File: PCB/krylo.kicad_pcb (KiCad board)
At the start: 2 copper layers, 135.3 x 87.6 mm, 52 parts, among them SW1 Switch, SW10 Switch, SW11 Switch, SW12 Switch, SW13 Switch, SW14 Switch, SW15 Switch, SW16 Switch, SW2 Switch, SW3 Switch, SW4 Switch, SW5 Switch, SW6 Switch, SW7 Switch, SW8 Switch, SW9 Switch, U1 nice_nano

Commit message: Fix: added the missing connection of the left backside power jumper
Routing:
- net Net-(SW_PWR1-B_back): track 27.3 -> 29.0 mm, vias 1 -> 2
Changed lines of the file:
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@@
 		)
 		(fp_line
-			(start 1.999998 -4.25)
+			(start 1.999997 -4.25)
 			(end 2 -7.7)
 			(stroke
@@
 		(fp_line
 			(start -1.5 -3.7)
-			(end 0.999998 -3.7)
+			(end 0.999997 -3.7)
 			(stroke
 				(width 0.1)
@@
 		)
 		(fp_arc
-			(start 0.999998 -3.7)
+			(start 0.999997 -3.7)
 			(mid 2.06066 -3.26066)
 			(end 2.5 -2.2)
@@
 		(net "Net-(SW_PWR1-B_back)")
 	)
+	(segment
+		(start 108.305185 105.254425)
+		(end 107.05038 103.99962)
+		(width 0.25)
+		(layer "F.Cu")
+		(net "Net-(SW_PWR1-B_back)")
+	)
+	(via
+		(at 107.05038 103.99962)
+		(size 0.6)
+		(drill 0.3)
+		(layers "F.Cu" "B.Cu")
+		(net "Net-(SW_PWR1-B_back)")
+	)
 	(via
 		(at 104.3 82.25)
@@
 	(segment
 		(start 108.325 105.27424)
-		(end 107.025 103.97424)
+		(end 107.05038 103.99962)
 		(width 0.25)
 		(layer "B.Cu")
@@
 		(width 0.25)
 		(layer "B.Cu")
+		(net "Net-(SW_PWR1-B_back)")
+	)
+	(segment
+		(start 107.05038 103.99962)
+		(end 107.025 103.97424)
+		(width 0.25)
+		(layer "B.Cu")

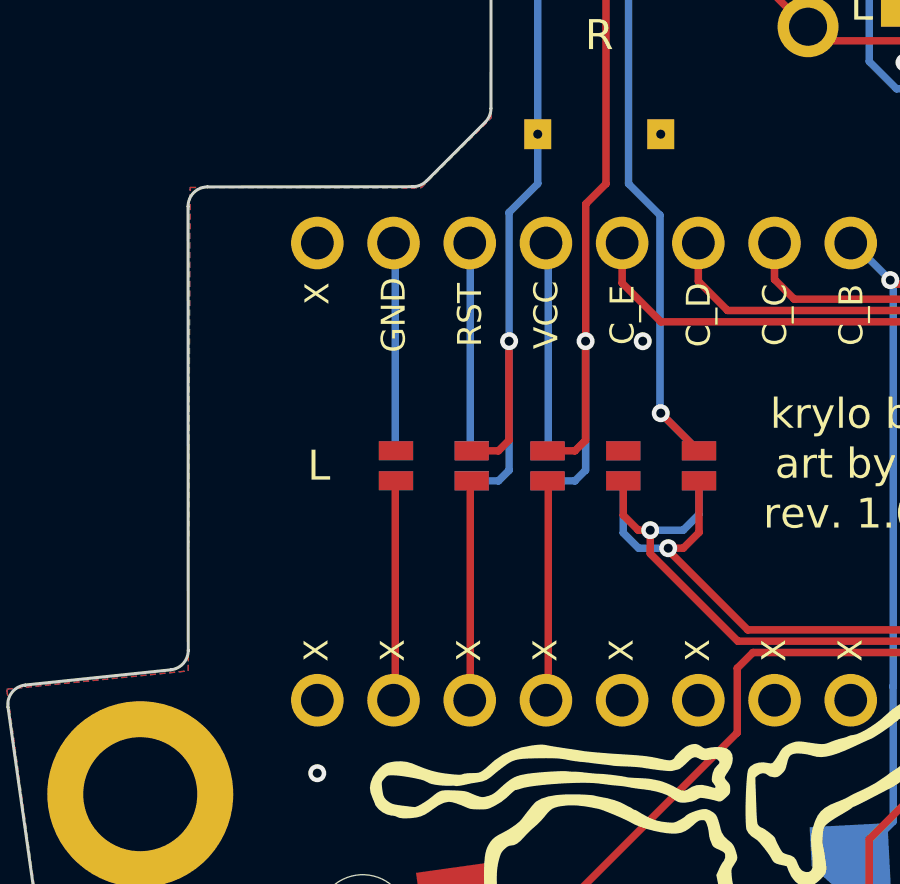
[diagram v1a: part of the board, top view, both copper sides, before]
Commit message: Fix: power goes to the VBAT pin instead of the EXT_GCC, this way we fix the inability to read the battery values by the MCU and avoid the soft off charge drain issue
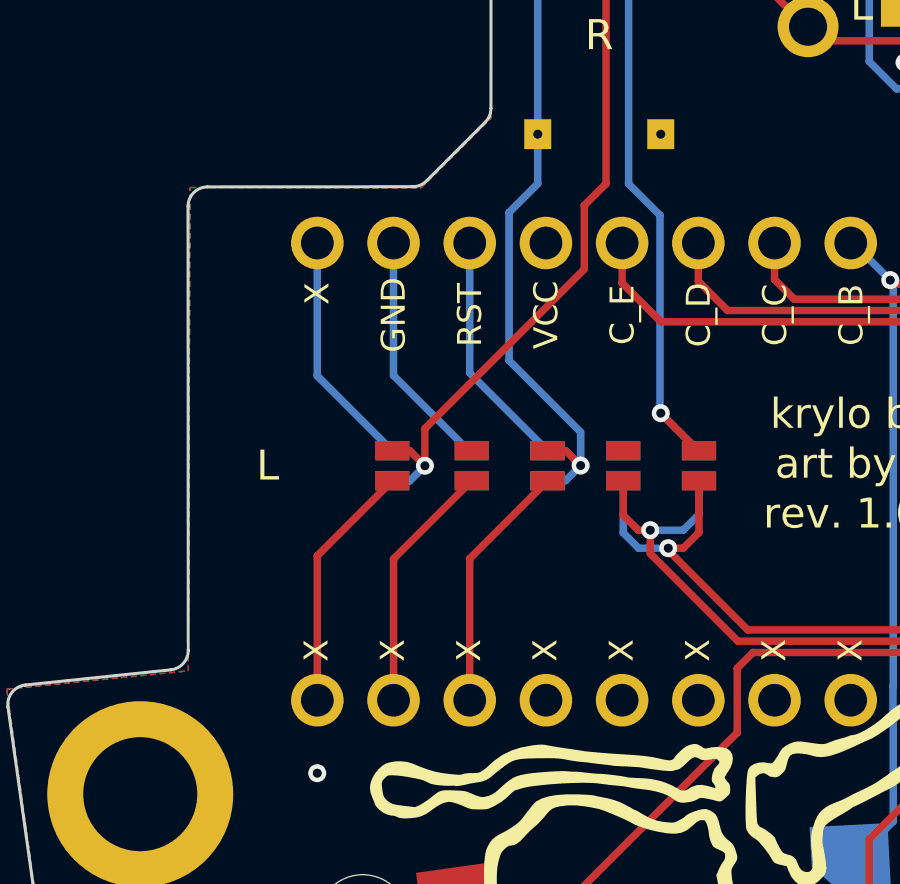
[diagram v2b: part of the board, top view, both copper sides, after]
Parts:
- moved JP9 5.18 mm to (98.1, 105.7)
- moved JP10 5.17 mm to (98.1, 105.8)
- moved JP7 2.53 mm to (103.3, 105.7)
- moved JP8 2.53 mm to (103.3, 105.8)
- moved JP5 2.52 mm to (100.7, 105.7)
- moved JP6 2.52 mm to (100.7, 105.7)
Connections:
- U1 pad 1: unconnected-(U1-D1/P0.06-Pad1) -> /+BATT_{indirect}
- U1 pad 13: unconnected-(U1-VBAT-Pad13) -> /+BATT_{indirect}
- U1 pad 16: /+BATT_{indirect} -> unconnected-(U1-EXT_VCC-Pad16)
- U1 pad 4: /+BATT_{indirect} -> unconnected-(U1-GND-Pad4)
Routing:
- net /RESET_{indirect}: track 13.7 -> 16.4 mm
- net RESET: track 24.3 -> 21.8 mm
- net /GND_{indirect}: track 14.0 -> 16.4 mm
- net /+BATT_{indirect}: track 13.8 -> 16.2 mm
- net +BATT: track 33.1 -> 31.7 mm
- net GND: vias 4 -> 3

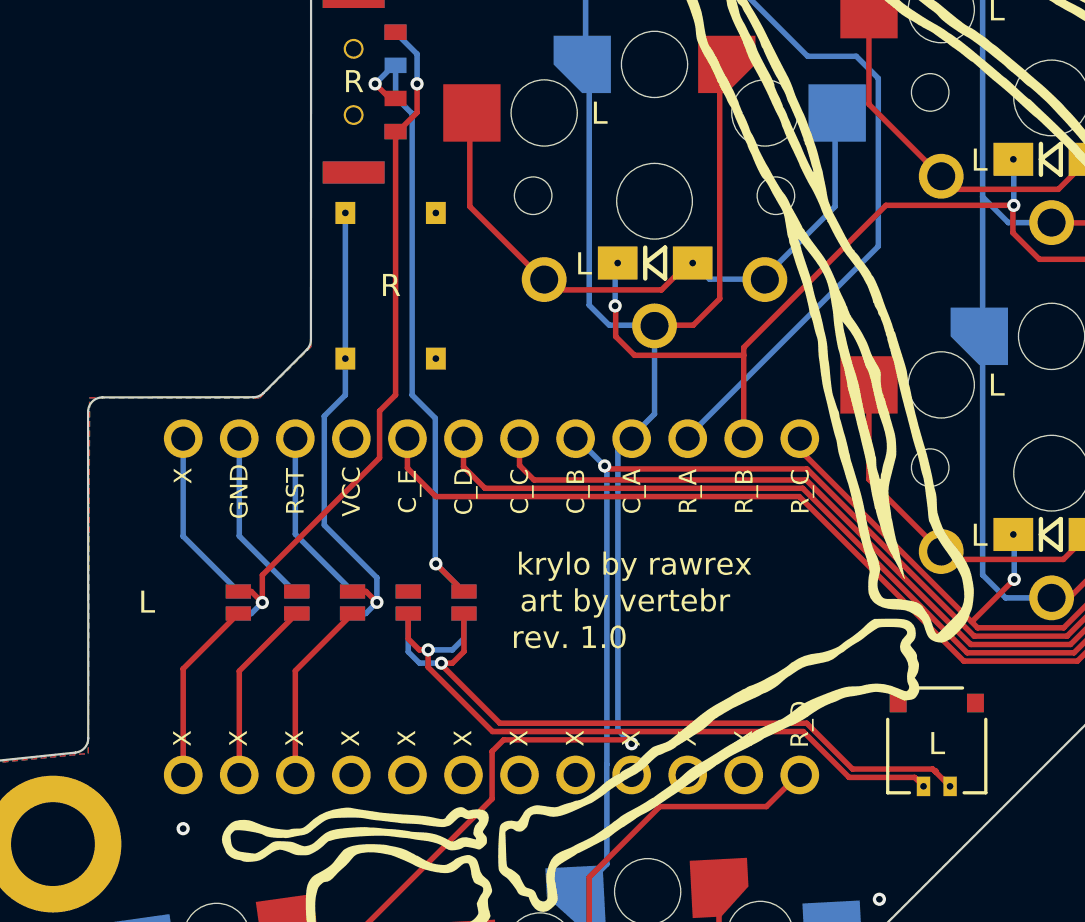
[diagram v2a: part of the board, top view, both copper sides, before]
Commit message: Jumper pads narrowed down and track clean up
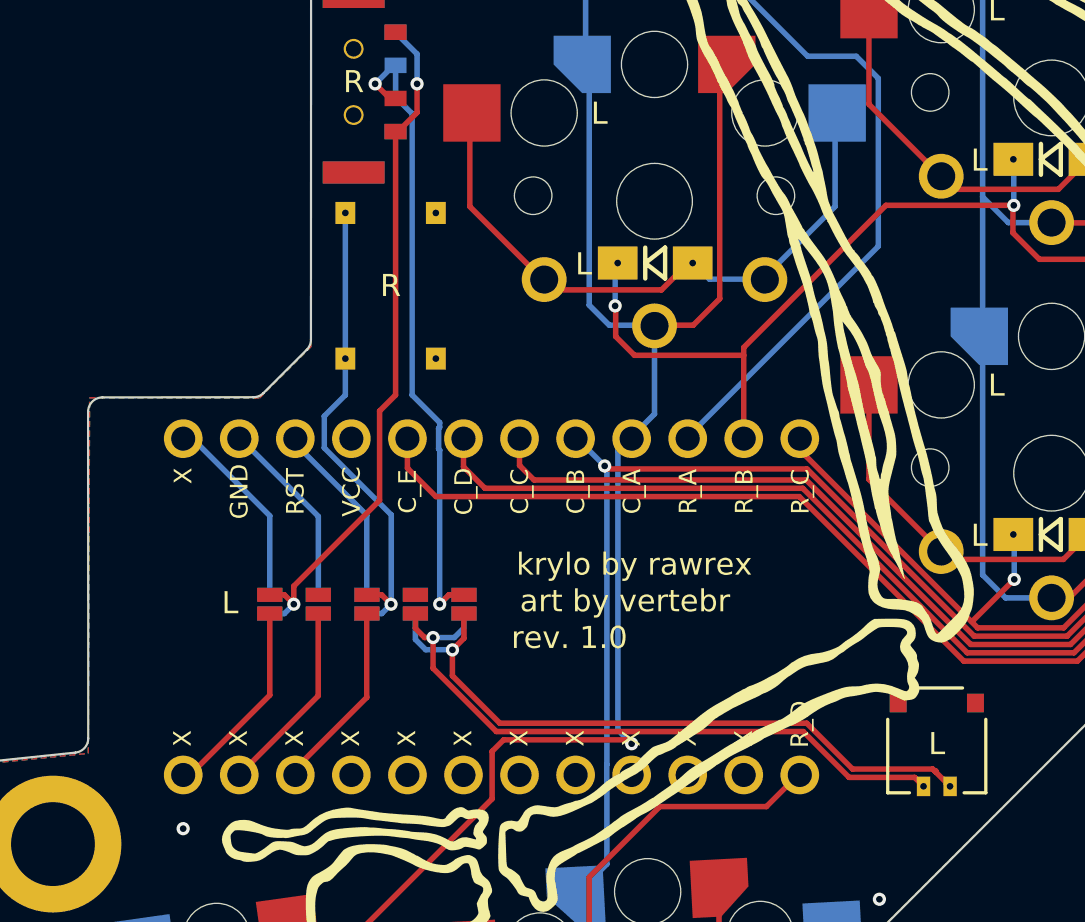
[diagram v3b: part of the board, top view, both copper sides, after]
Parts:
- BT1: value MOLEX_C -> Molex
- H1, H2, H3, H4: value Mount -> SMTSO2020MTJ_M2
- moved JP10 1.43 mm to (99.5, 105.9)
- moved JP9 1.43 mm to (99.5, 105.8)
- moved JP6 0.99 mm to (101.7, 105.9)
- moved JP5 0.98 mm to (101.7, 105.8)
- moved JP8 0.67 mm to (103.9, 105.9)
- moved JP7 0.65 mm to (103.9, 105.8)
- moved JP1 0.33 mm to (106.1, 105.8)
- moved JP4 0.33 mm to (106.1, 105.8)
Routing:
- net /PAD1: track 31.8 -> 30.7 mm
- net /PAD2: track 30.7 -> 29.7 mm
- net /+BATT_{indirect}: track 16.2 -> 17.1 mm
- net Net-(SW_PWR1-B_back): track 29.0 -> 30.0 mm
- net /GND_{indirect}: track 16.4 -> 17.2 mm
- net +BATT: track 31.7 -> 31.1 mm

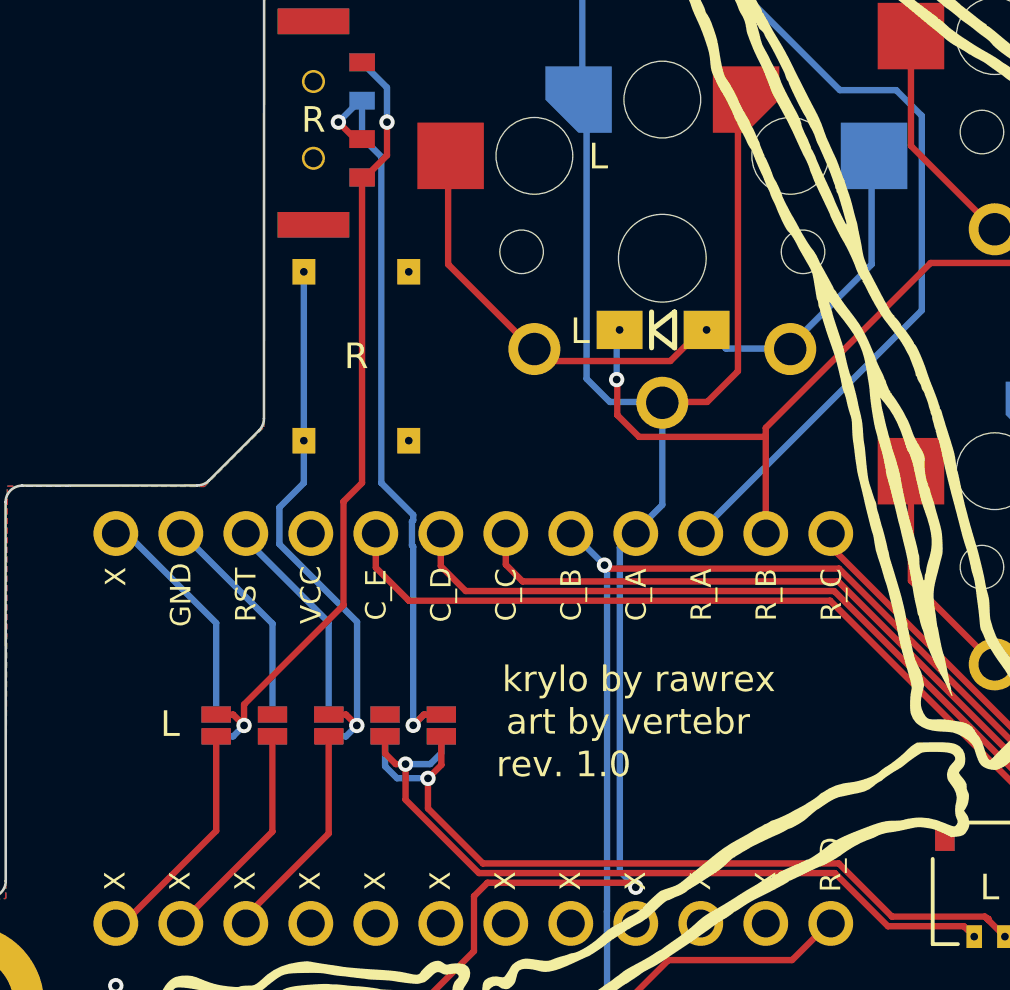
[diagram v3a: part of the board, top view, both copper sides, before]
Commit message: Clean ups and alignments after the jumpers narrowing and moving
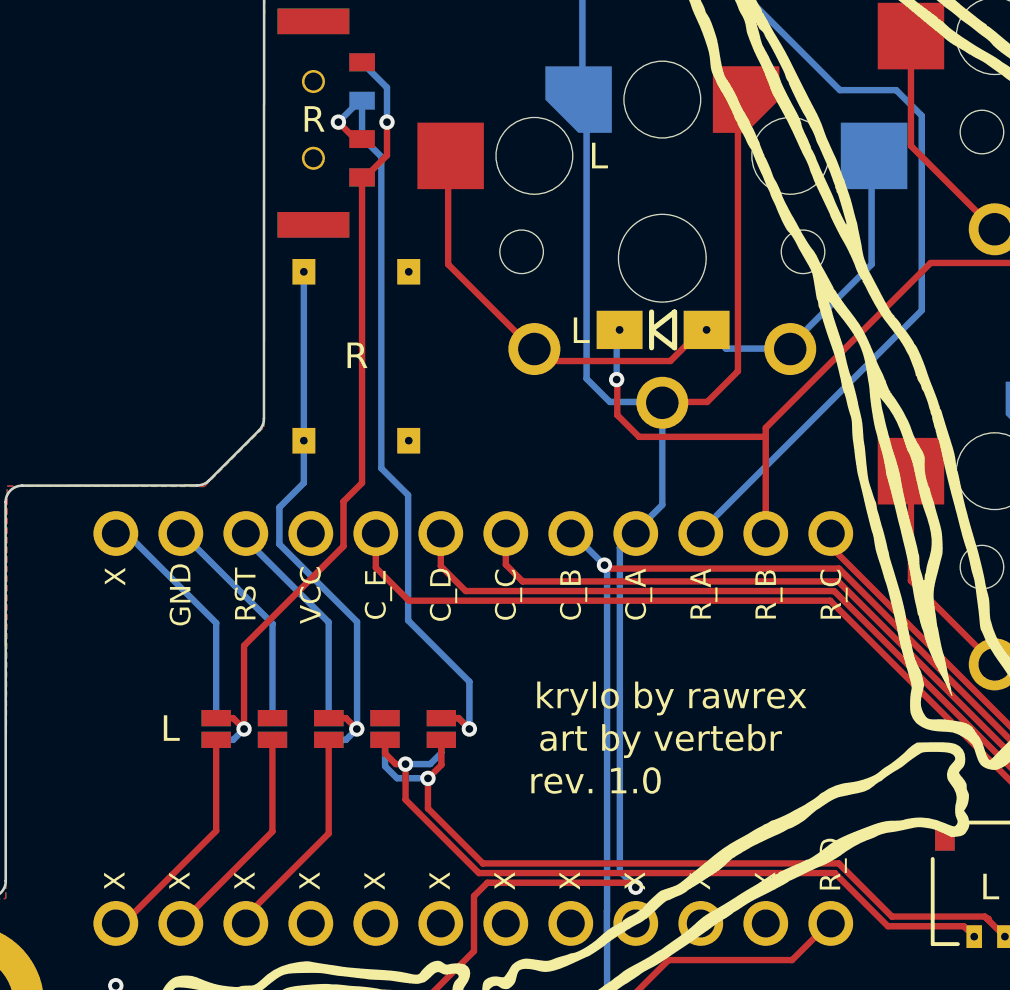
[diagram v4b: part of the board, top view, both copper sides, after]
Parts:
- moved INFO 1.42 mm to (116.8, 106.0)
- moved JP1 0.14 mm to (106.1, 105.9)
- moved JP3 0.14 mm to (108.3, 105.9)
- moved JP7 0.14 mm to (103.9, 105.9)
- moved JP10 0.14 mm to (99.5, 106.0)
- moved JP2 0.14 mm to (108.3, 105.9)
- moved JP4 0.14 mm to (106.1, 105.9)
- moved JP5 0.14 mm to (101.7, 105.9)
- moved JP6 0.14 mm to (101.7, 106.0)
- moved JP8 0.14 mm to (103.9, 106.0)
- moved JP9 0.14 mm to (99.5, 105.9)
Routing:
- net Net-(SW_PWR1-B_back): track 30.0 -> 31.0 mm
